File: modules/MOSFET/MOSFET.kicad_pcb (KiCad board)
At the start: 2 copper layers, 40.6 x 40.6 mm, 34 parts, among them J1 2, J10 11, J11 12, J12 13, J13 A0, J14 A1, J15 A2, J16 A3, J17 A4, J18 A5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

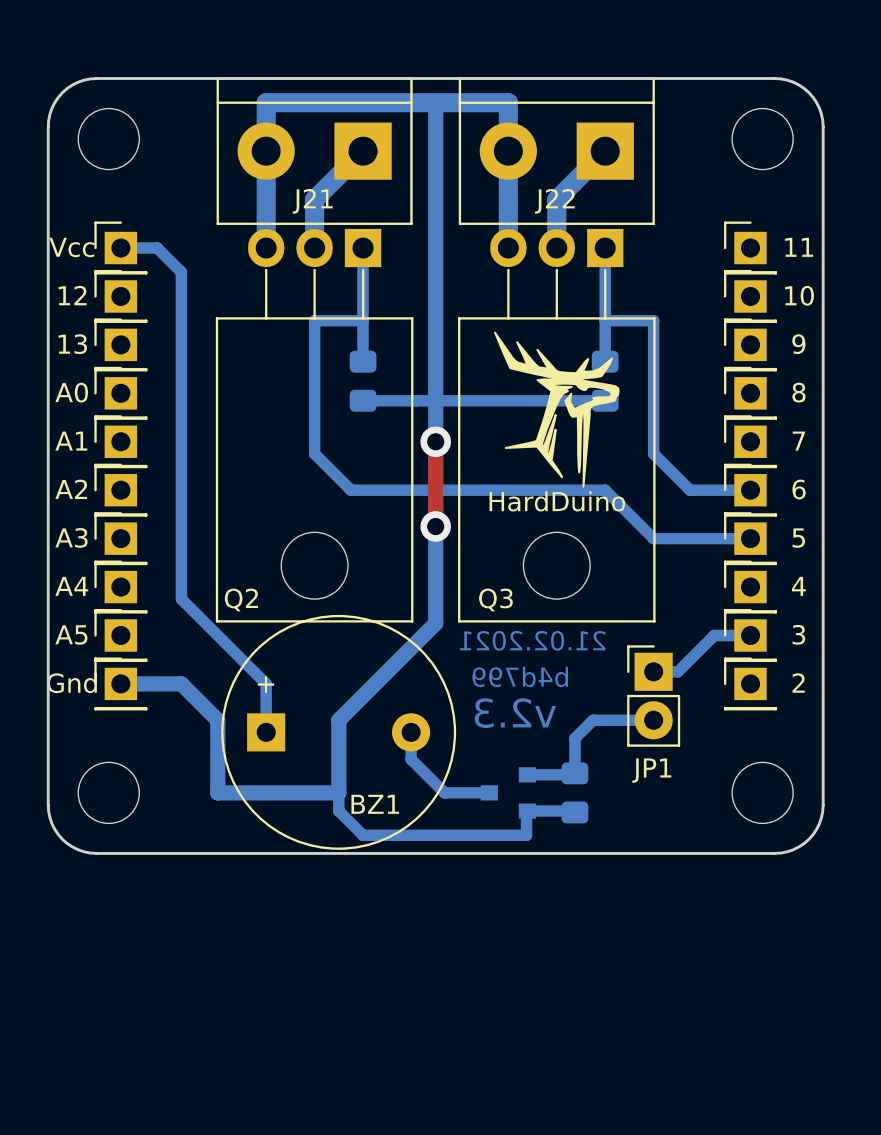
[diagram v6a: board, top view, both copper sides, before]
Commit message: All 1x shields was rotated clockwise
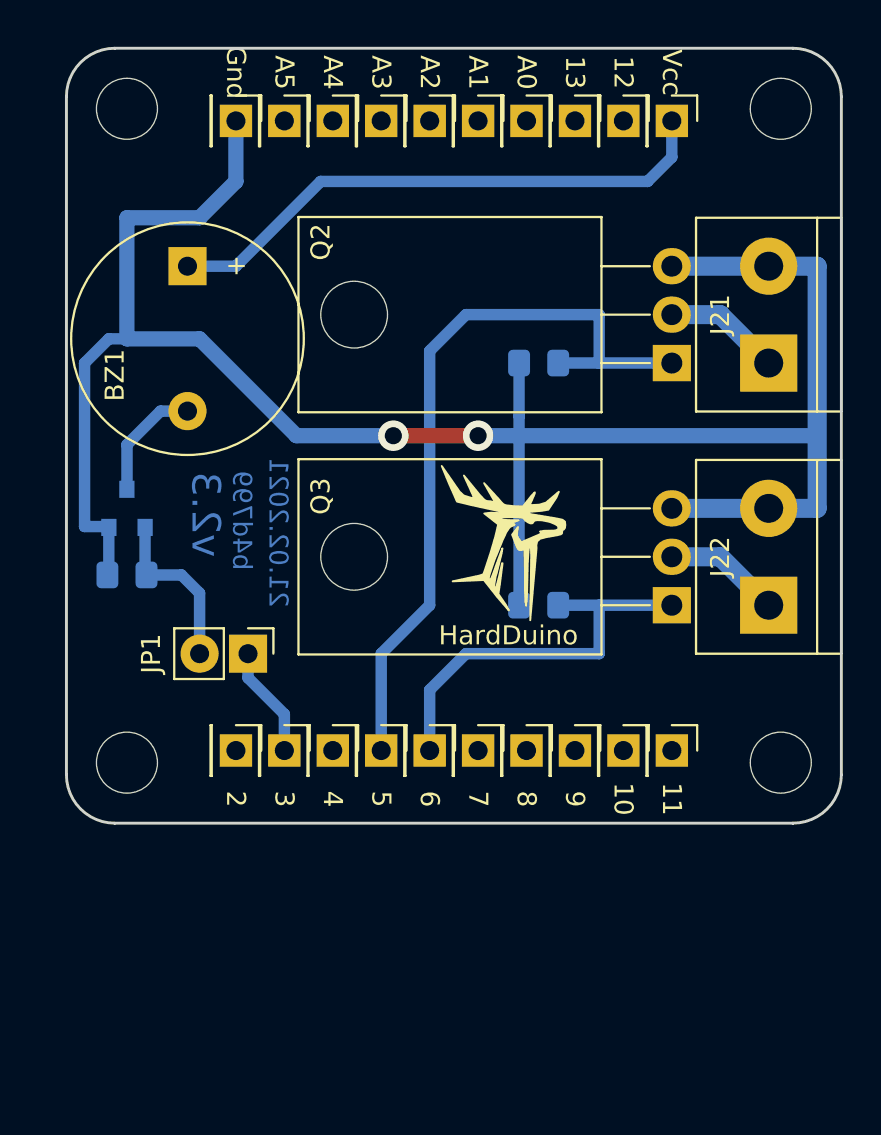
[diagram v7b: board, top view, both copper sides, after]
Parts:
- moved H2 35.9 mm to (93.0, 39.7), turned to 270 degrees
- moved H1 35.3 mm to (127.3, 39.7), turned to 270 degrees
- moved H4 33.4 mm to (93.0, 74.0), turned to 270 degrees
- moved H3 32.7 mm to (127.3, 74.0), turned to 270 degrees
- moved J20 30.1 mm to (98.7, 40.3), turned to 270 degrees
- moved J19 29.7 mm to (121.6, 40.3), turned to 270 degrees
- moved J18 28.3 mm to (101.3, 40.3), turned to 270 degrees
- moved J11 27.9 mm to (119.1, 40.3), turned to 270 degrees
- moved J1 27.2 mm to (98.7, 73.3), turned to 270 degrees
- moved J17 26.9 mm to (103.8, 40.3), turned to 270 degrees
- moved J10 26.7 mm to (121.6, 73.3), turned to 270 degrees
- moved J12 26.6 mm to (116.5, 40.3), turned to 270 degrees
- moved R1 26.1 mm to (93.0, 64.1), turned to 180 degrees
- moved J16 25.8 mm to (106.4, 40.3), turned to 270 degrees
- moved J13 25.6 mm to (114.0, 40.3), turned to 270 degrees
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
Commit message: Now all mounting holes have distance 31.92 x 31.1
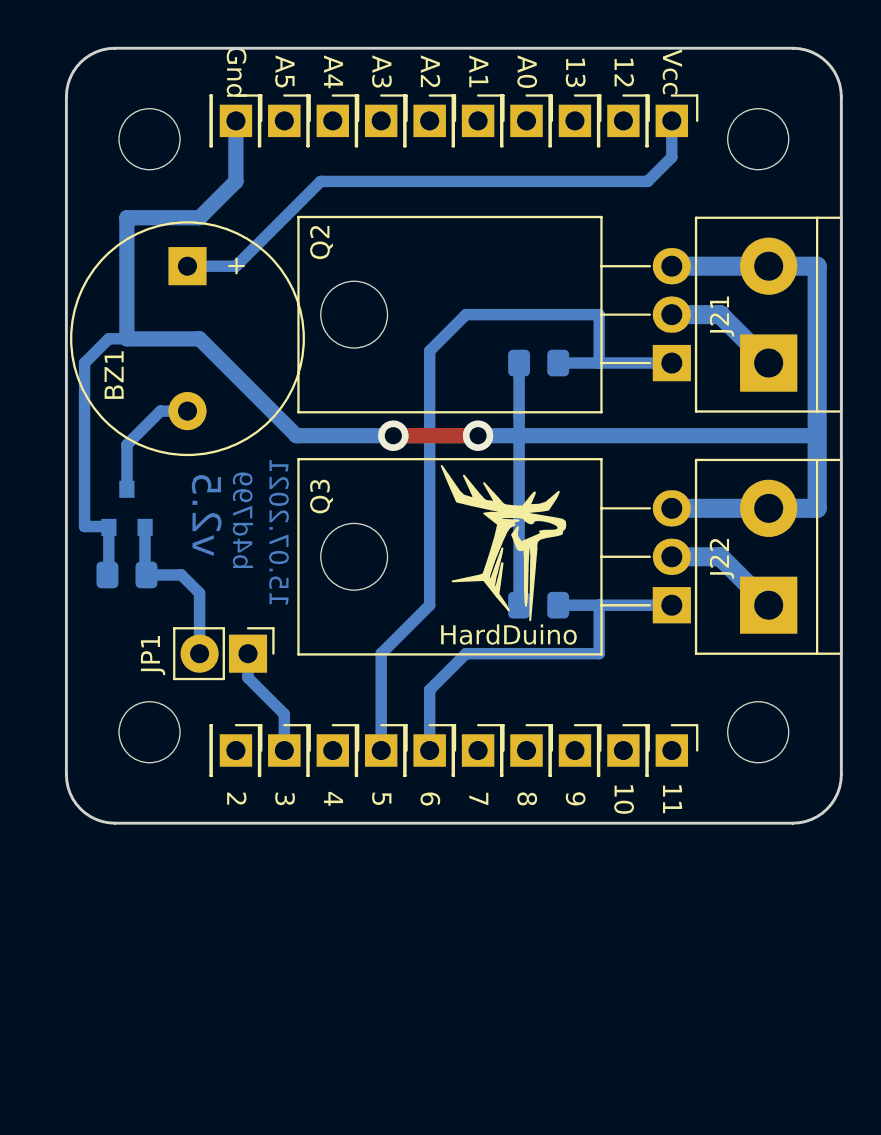
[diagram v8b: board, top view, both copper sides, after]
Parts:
- moved H3 1.99 mm to (126.1, 72.4), turned to 0 degrees
- moved H4 1.99 mm to (94.2, 72.4), turned to 0 degrees
- moved H1 1.99 mm to (126.1, 41.3), turned to 0 degrees
- moved H2 1.99 mm to (94.2, 41.3), turned to 0 degrees
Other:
- board text added: "15.07.2021"
- board text added: "v2.5"
- board text removed: "21.02.2021"
- board text removed: "v2.3"
